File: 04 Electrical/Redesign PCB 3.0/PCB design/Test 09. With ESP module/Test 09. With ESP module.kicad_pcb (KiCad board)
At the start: 2 copper layers, 90 x 54 mm, 69 parts, among them J1 USB-C port, J2 Boiler, J3 Test connector, Q1 MMBT2907A, Q2 LBSS138LT1G-ES, SW1 btn_home, SW2 btn_up, SW3 btn_down, SW4 btn_confirm, SW5 btn_back, U1 ESP32-S3-WROOM-1-N8R2, U10 LP5907MFX-2.8/NOPB, U11 VL53L0CXV0DH/1, U2 SGM2212-3.3XKC3G/TR, U3 EL357N-G, U4 EL357N-G, U5 ILI9341_no_touch, U6 DS18S20, U7 DS18S20, U8 DS18S20, U9 DS18S20

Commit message: Routing PCB test 9
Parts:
- removed C13: 10u, Capacitor_SMD:C_0402_1005Metric
- removed C14: 0.1u, Capacitor_SMD:C_0603_1608Metric
- removed C15: 4.7pF, Capacitor_SMD:C_0603_1608Metric
- removed D18, D19, D20: WS2812B-2020, LED_SMD:LED_WS2812B_PLCC4_5.0x5.0mm_P3.2mm
- removed Q2: LBSS138LT1G-ES, Package_TO_SOT_SMD:SOT-23
- removed R11, R12, R13: 10k, Resistor_SMD:R_0603_1608Metric
- removed U10: LP5907MFX-2.8/NOPB, Package_TO_SOT_SMD:SOT-23-5
- removed U11: VL53L0CXV0DH/1, Sensor_Distance:ST_VL53L1x
- added J4: VL6180, Connector_PinHeader_2.00mm:PinHeader_1x06_P2.00mm_Vertical, F.Cu at (169.5, 50.5)
- J3: footprint Project:PinHeader_1x04_P2.54mm_Horizontal -> Connector_PinHeader_2.54mm:PinHeader_1x06_P2.54mm_Vertical
- U3, U4: footprint EL357N-G:OPTO_EL357N-G -> Package_SO:SOP-4_3.8x4.1mm_P2.54mm
- moved J3 10.8 mm to (148.4, 99.8)
- moved R3 7.41 mm to (118.0, 96.5), turned to 0 degrees
- moved R2 7.35 mm to (132.8, 96.8), turned to 180 degrees
- moved J2 6.97 mm to (167.7, 98.6)
- moved C10 5.76 mm to (160.8, 87.6)
- moved D11 5.76 mm to (163.3, 87.6)
- moved D6 5.76 mm to (155.1, 94.3)
- moved D8 5.76 mm to (160.1, 94.3)
- moved Q1 5.76 mm to (154.8, 87.6)
- moved R7 5.76 mm to (158.3, 87.6)
- moved C11 5.76 mm to (150.0, 80.7)
- moved C12 5.76 mm to (166.0, 81.0)
- moved C9 5.76 mm to (149.9, 87.9)
- moved D10 5.76 mm to (149.9, 90.4)
- moved D12 5.76 mm to (167.6, 90.3)
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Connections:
- D6 pad 2: Net-(D6-A) -> Boiler 1
- D7 pad 1: Net-(D6-A) -> Boiler 1
- D8 pad 2: Net-(D8-A) -> Boiler 2
- D9 pad 1: Net-(D8-A) -> Boiler 2
- J2 pad 1: Net-(D6-A) -> Boiler 1
- J2 pad 2: Net-(D8-A) -> Boiler 2
- U1 pad 11: Disp_LED -> unconnected-(U1-GPIO18/U1RXD/ADC2_CH7/CLK_OUT3-Pad11)
- U1 pad 15: Disp_CS -> Disp_LED
- U1 pad 16: Disp_MISO -> unconnected-(U1-GPIO46-Pad16)
- U1 pad 17: Disp_SCK -> unconnected-(U1-GPIO9/TOUCH9/ADC1_CH8/FSPIHD/SUBSPIHD-Pad17)
- U1 pad 18: Disp_MOSI -> unconnected-(U1-GPIO10/TOUCH10/ADC1_CH9/FSPICS0/FSPIIO4/SUBSPICS0-Pad18)
- U1 pad 19: unconnected-(U1-GPIO11/TOUCH11/ADC2_CH0/FSPID/FSPIIO5/SUBSPID-Pad19) -> Disp_MOSI
- U1 pad 20: TOF_SCL -> Disp_SCK
- U1 pad 21: TOF_XSHUT -> Disp_MISO
- U1 pad 22: TOF_GPIO01 -> unconnected-(U1-GPIO14/TOUCH14/ADC2_CH3/FSPIWP/FSPIDQS/SUBSPIWP-Pad22)
- U1 pad 23: TOF_SDA -> unconnected-(U1-GPIO21-Pad23)
- U1 pad 27: unconnected-(U1-GPIO0/BOOT-Pad27) -> btn_back
- U1 pad 28: unconnected-(U1-SPIIO6/GPIO35/FSPID/SUBSPID-Pad28) -> btn_confirm
- U1 pad 29: unconnected-(U1-SPIIO7/GPIO36/FSPICLK/SUBSPICLK-Pad29) -> SD_CS
- U1 pad 30: btn_back -> SD_MOSI
- U1 pad 31: btn_confirm -> SD_MISO
- U1 pad 32: SD_CS -> SD_SCK
- U1 pad 33: SD_MOSI -> btn_down
- U1 pad 34: SD_MISO -> btn_up
- U1 pad 35: SD_SCK -> btn_home
- U1 pad 36: btn_down -> TOF_SDA
- U1 pad 37: btn_up -> TOF_SCL
- U1 pad 38: btn_home -> TOF_GPIO01
- U1 pad 39: WS2812_CTRL -> TOF_XSHUT
- U1 pad 7: Disp_RES -> Disp_CS
- U1 pad 8: Disp_DC -> Disp_RES
- U1 pad 9: unconnected-(U1-GPIO16/U0CTS/ADC2_CH5/XTAL_32K_N-Pad9) -> Disp_DC
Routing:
- net VCC_5V: track 123.5 -> 46.6 mm, vias 2 -> 1
- net Boiler 1: track 0.00 -> 45.1 mm, vias 0 -> 2
- net VCC_3V3: track 298.6 -> 260.4 mm, vias 13 -> 6
- net Boiler 2: track 0.00 -> 37.9 mm, vias 0 -> 2
- net Net-(U10-OUT): track 23.4 -> 0.00 mm
- net Net-(D6-A): track 22.1 -> 0.00 mm
- net WS2812_CTRL: track 22.0 -> 0.00 mm
- net Net-(D8-A): track 14.5 -> 0.00 mm
- net Net-(D18-DIN): track 7.28 -> 0.00 mm
- net TOF_GPIO01: track 42.7 -> 36.0 mm
- net boil_to_cntr: track 38.8 -> 32.3 mm
- net btn_down: track 64.6 -> 58.1 mm
- net Net-(D18-DOUT): track 5.51 -> 0.00 mm
- net Net-(D19-DOUT): track 5.43 -> 0.00 mm
- net TOF_SDA: track 45.0 -> 40.3 mm
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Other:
- board text added: "Boiler 1"
- board text added: "Boiler 2"
- board text added: "GPIO01"
- board text added: "SCL"
- board text added: "SDA"
- board text added: "XSHUT"

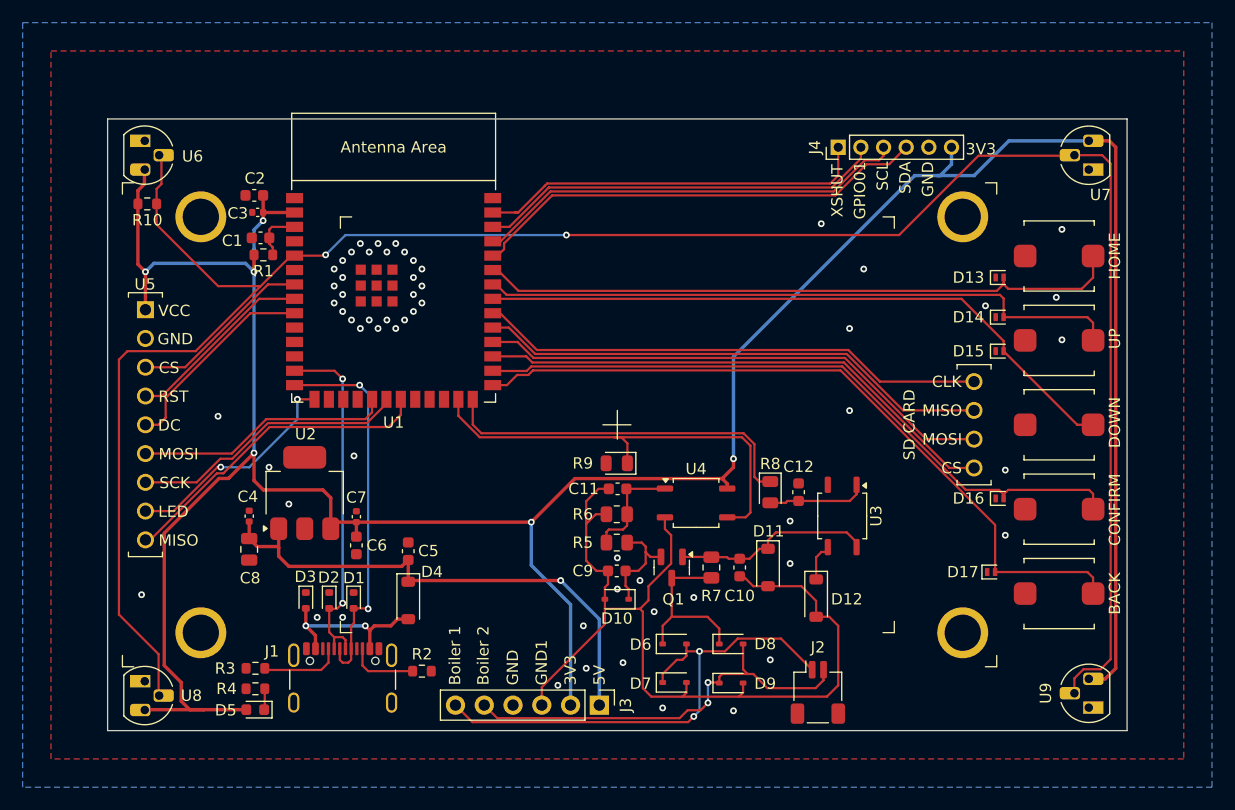
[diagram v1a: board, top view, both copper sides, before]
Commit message: Logo added to PCB
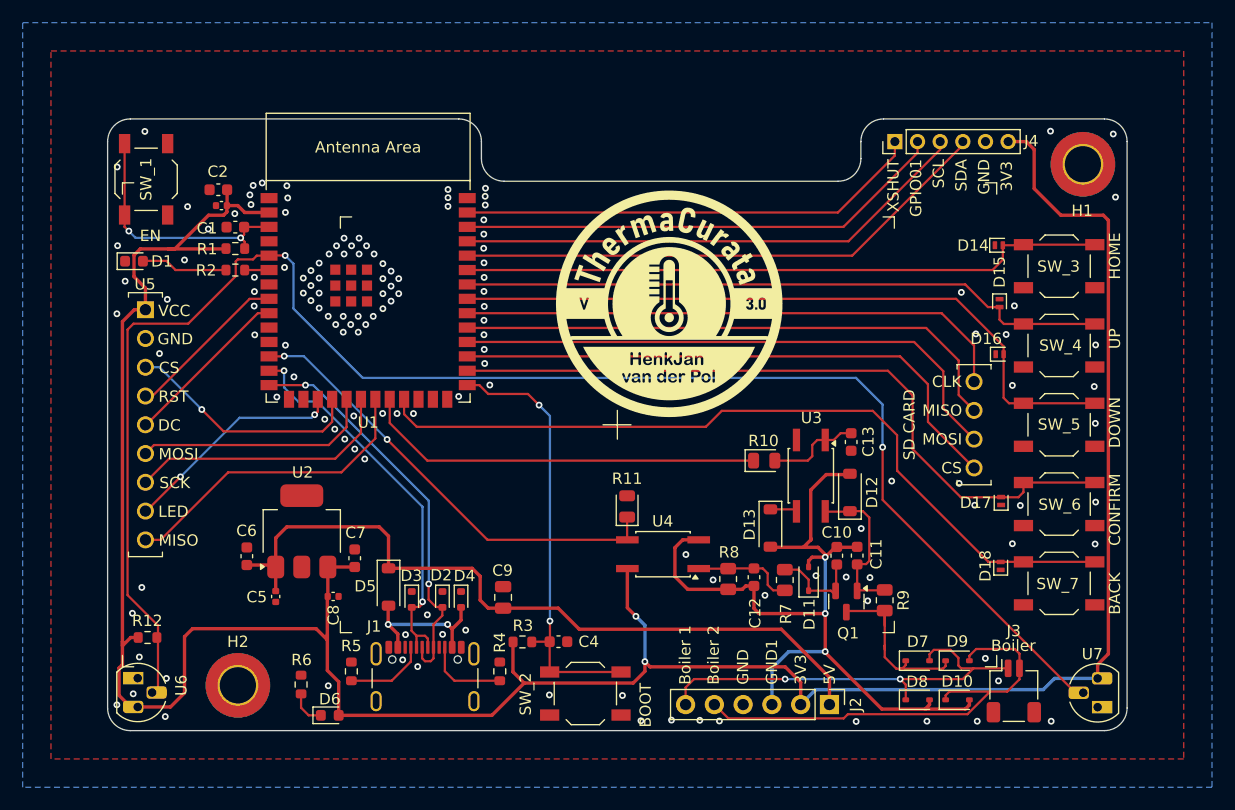
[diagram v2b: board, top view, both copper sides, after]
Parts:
- removed SW1: btn_home, Project:SW_Push_SPEH
- removed SW2: btn_up, Project:SW_Push_SPEH
- removed SW3: btn_down, Project:SW_Push_SPEH
- removed SW4: btn_confirm, Project:SW_Push_SPEH
- removed SW5: btn_back, Project:SW_Push_SPEH
- removed U8, U9: DS18S20, Package_TO_SOT_THT:TO-92L_HandSolder
- added C13: 2n2, Capacitor_SMD:C_0603_1608Metric, F.Cu at (170.6, 76.5)
- added D18: LESD8D3.3CAT5G-ES, Diode_SMD:D_SOD-882, F.Cu at (183.8, 87.5)
- added H1: MountingHole_Pad, MountingHole:MountingHole_3.2mm_M3_ISO7380_Pad_TopBottom, F.Cu at (191.1, 52.0)
- added H2: MountingHole_Pad, MountingHole:MountingHole_3.2mm_M3_ISO7380_Pad_TopBottom, F.Cu at (116.5, 98.0)
- added R11: 330, Diode_SMD:D_0805_2012Metric, F.Cu at (150.9, 82.2)
- added R12: 4k7, Resistor_SMD:R_0603_1608Metric, F.Cu at (108.5, 93.8)
- added SW_1: EN, Button_Switch_SMD:SW_SPST_TL3342, F.Cu at (108.4, 53.3)
- added SW_2: BOOT, Button_Switch_SMD:SW_SPST_TL3342, F.Cu at (147.2, 98.7)
- added SW_3: HOME, Button_Switch_SMD:SW_SPST_TL3342, F.Cu at (189.0, 61.0)
- added SW_4: UP, Button_Switch_SMD:SW_SPST_TL3342, F.Cu at (189.0, 68.0)
- added SW_5: DOWN, Button_Switch_SMD:SW_SPST_TL3342, F.Cu at (189.0, 75.0)
- added SW_6: CONFIRM, Button_Switch_SMD:SW_SPST_TL3342, F.Cu at (189.0, 82.0)
- added SW_7: BACK, Button_Switch_SMD:SW_SPST_TL3342, F.Cu at (189.0, 89.0)
- C10, C12: value 2n2 -> 10n
- C11: value 10n -> 2n2
- C4: value 10u -> 1u; footprint Capacitor_SMD:C_0402_1005Metric -> Capacitor_SMD:C_0603_1608Metric
- C5: value 0.1u -> 10u; footprint Capacitor_SMD:C_0603_1608Metric -> Capacitor_SMD:C_0402_1005Metric
- C7: value 10u -> 0.1u; footprint Capacitor_SMD:C_0402_1005Metric -> Capacitor_SMD:C_0603_1608Metric
- C8: value 22u -> 10u; footprint Capacitor_SMD:C_0805_2012Metric -> Capacitor_SMD:C_0402_1005Metric
- C9: value 10n -> 22u; footprint Capacitor_SMD:C_0603_1608Metric -> Capacitor_SMD:C_0805_2012Metric
- D1: value LESD5D5.0CT1G -> XL-1608UGC-04; footprint Diode_SMD:D_SOD-523 -> LED_SMD:LED_0603_1608Metric
- D10: value BZT52C4V7S -> 1N4148WS
- D11: value BZT52C15V -> BZT52C4V7S; footprint Diode_SMD:D_SOD-123 -> Diode_SMD:D_SOD-323
- D12: value BZT52C4V3 -> BZT52C15V
- D13: value LESD8D3.3CAT5G-ES -> BZT52C4V3; footprint Diode_SMD:D_SOD-882 -> Diode_SMD:D_SOD-123
- D4: value 1N5819HW-7-F -> LESD5D5.0CT1G; footprint Diode_SMD:D_SOD-123 -> Diode_SMD:D_SOD-523
- D5: value XL-1608UGC-04 -> 1N5819HW-7-F; footprint LED_SMD:LED_0603_1608Metric -> Diode_SMD:D_SOD-123
- D6: value 1N4148WS -> XL-1608UGC-04; footprint Diode_SMD:D_SOD-323 -> LED_SMD:LED_0603_1608Metric
- J2: value Boiler -> Test connector; footprint Connector_JST:JST_SH_SM02B-SRSS-TB_1x02-1MP_P1.00mm_Horizontal -> Connector_PinHeader_2.54mm:PinHeader_1x06_P2.54mm_Vertical
- J3: value Test connector -> Boiler; footprint Connector_PinHeader_2.54mm:PinHeader_1x06_P2.54mm_Vertical -> Connector_JST:JST_SH_SM02B-SRSS-TB_1x02-1MP_P1.00mm_Horizontal
- R10: value 4k7 -> 1k5; footprint Resistor_SMD:R_0603_1608Metric -> Diode_SMD:D_0805_2012Metric
- R2: value 4k7 -> 5k1
- R3: value 4k7 -> 10k
- R4: value 5k1 -> 4k7
- R5: value 200 -> 4k7; footprint Resistor_SMD:R_0805_2012Metric -> Resistor_SMD:R_0603_1608Metric
- R6: value 150 -> 5k1; footprint Resistor_SMD:R_0805_2012Metric -> Resistor_SMD:R_0603_1608Metric
- R7: value 330 -> 200
- R8: value 1k5 -> 150; footprint Diode_SMD:D_0805_2012Metric -> Resistor_SMD:R_0805_2012Metric
- R9: footprint Diode_SMD:D_0805_2012Metric -> Resistor_SMD:R_0805_2012Metric
- U3, U4: footprint Package_SO:SOP-4_3.8x4.1mm_P2.54mm -> Package_SO:SO-4_4.4x3.6mm_P2.54mm
- U5: footprint Project:ILI9341_no_touch -> Project:ILI9341_no_touch_no_mount
- moved R10 59.0 mm to (163.0, 78.2), turned to 0 degrees
- moved U7 47.5 mm to (192.4, 99.9)
- moved U6 47.4 mm to (107.7, 97.4)
- moved R2 39.1 mm to (116.3, 61.3), turned to 0 degrees
- moved J3 36.6 mm to (185.0, 98.5), turned to 0 degrees
- moved D1 35.7 mm to (107.3, 60.6), turned to 0 degrees
- moved R6 31.7 mm to (122.1, 97.9), turned to -90 degrees
- moved D10 31.4 mm to (180.0, 99.3), turned to 0 degrees
- moved D6 31.1 mm to (124.6, 100.7)
- moved D13 30.0 mm to (163.5, 84.1), turned to -90 degrees
- moved C4 29.5 mm to (144.8, 94.2), turned to 0 degrees
- moved R9 26.6 mm to (173.6, 90.5), turned to -90 degrees
- moved R5 26.0 mm to (126.5, 96.8), turned to -90 degrees
- moved R3 23.7 mm to (141.6, 94.2)
- moved C11 22.0 mm to (171.2, 86.5), turned to 90 degrees
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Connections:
- C10 pad 1: Net-(D11-K) -> GND1
- C10 pad 2: GND1 -> Net-(D11-K)
- C11 pad 1: GND1 -> Net-(D12-K)
- C11 pad 2: Net-(C11-Pad2) -> GND1
- C12 pad 1: GND -> GND1
- C4 pad 1: VCC_5V -> Net-(U1-GPIO0/BOOT)
- C6 pad 1: VCC_3V3 -> VCC_5V
- C8 pad 1: VCC_5V -> VCC_3V3
- C9 pad 1: GND1 -> VCC_5V
- C9 pad 2: Net-(D10-K) -> GND
- D1 pad 2: USB D+ -> Net-(D1-A)
- D10 pad 1: Net-(D10-K) -> Boiler 2
- D13 pad 1: GND -> Net-(D13-K)
- D13 pad 2: btn_home -> GND1
- D14 pad 2: btn_up -> btn_home
- D15 pad 2: btn_down -> btn_up
- D16 pad 2: btn_confirm -> btn_down
- D17 pad 2: btn_back -> btn_confirm
- D2 pad 2: USB D- -> USB D+
- D3 pad 2: Vusb -> USB D-
- D4 pad 1: VCC_5V -> GND
- D5 pad 1: Net-(D5-K) -> VCC_5V
- D5 pad 2: VCC_3V3 -> Vusb
- D6 pad 2: Boiler 1 -> VCC_3V3
- D7 pad 1: Boiler 1 -> Net-(D7-K)
- D7 pad 2: GND1 -> Boiler 1
- D8 pad 1: Net-(D6-K) -> Boiler 1
- D8 pad 2: Boiler 2 -> GND1
- D9 pad 1: Boiler 2 -> Net-(D7-K)
- D9 pad 2: GND1 -> Boiler 2
- J2 pad 1: Boiler 1 -> VCC_5V
- J2 pad 2: Boiler 2 -> VCC_3V3
- J3 pad 1: VCC_5V -> Boiler 1
- J3 pad 2: VCC_3V3 -> Boiler 2
- Q1 pad 1: Net-(D11-K) -> Net-(D12-K)
- Q1 pad 2: Net-(D10-K) -> Net-(D11-K)
- Q1 pad 3: Net-(D6-K) -> Net-(D7-K)
- R1 pad 1: Net-(U1-EN) -> VCC_3V3
- R1 pad 2: VCC_3V3 -> Net-(U1-EN)
- R10 pad 1: onewire -> boil_to_cntr
- R10 pad 2: VCC_3V3 -> Net-(C13-Pad2)
- R2 pad 1: GND -> Net-(D1-A)
- R2 pad 2: Net-(J1-CC2) -> Net-(U1-GPIO6/TOUCH6/ADC1_CH5)
- R3 pad 1: GND -> VCC_3V3
- R3 pad 2: Net-(J1-CC1) -> Net-(U1-GPIO0/BOOT)
- R4 pad 2: Net-(D5-K) -> Net-(J1-CC2)
- R5 pad 1: Net-(D10-K) -> GND
- R5 pad 2: Net-(C11-Pad2) -> Net-(J1-CC1)
- R6 pad 1: Net-(C11-Pad2) -> GND
- R6 pad 2: GND1 -> Net-(D6-K)
- R7 pad 2: Net-(D6-K) -> Net-(C12-Pad2)
- R8 pad 1: boil_to_cntr -> Net-(C12-Pad2)
- R8 pad 2: Net-(C12-Pad2) -> GND1
- R9 pad 1: cntr_to_boil -> Net-(D12-K)
- R9 pad 2: GND -> Net-(D7-K)
- U1 pad 12: unconnected-(U1-GPIO8/TOUCH8/ADC1_CH7/SUBSPICS1-Pad12) -> cntr_to_boil
- U1 pad 15: Disp_LED -> unconnected-(U1-GPIO3/TOUCH3/ADC1_CH2-Pad15)
- U1 pad 17: unconnected-(U1-GPIO9/TOUCH9/ADC1_CH8/FSPIHD/SUBSPIHD-Pad17) -> Disp_LED
- U1 pad 18: unconnected-(U1-GPIO10/TOUCH10/ADC1_CH9/FSPICS0/FSPIIO4/SUBSPICS0-Pad18) -> Disp_CS
- U1 pad 22: unconnected-(U1-GPIO14/TOUCH14/ADC2_CH3/FSPIWP/FSPIDQS/SUBSPIWP-Pad22) -> boil_to_cntr
- U1 pad 23: unconnected-(U1-GPIO21-Pad23) -> btn_back
- U1 pad 25: cntr_to_boil -> unconnected-(U1-GPIO48/SPICLK_N/SUBSPICLK_N_DIFF-Pad25)
- U1 pad 26: boil_to_cntr -> unconnected-(U1-GPIO45-Pad26)
- U1 pad 27: btn_back -> Net-(U1-GPIO0/BOOT)
- U1 pad 6: unconnected-(U1-GPIO6/TOUCH6/ADC1_CH5-Pad6) -> Net-(U1-GPIO6/TOUCH6/ADC1_CH5)
- U1 pad 7: Disp_CS -> unconnected-(U1-GPIO7/TOUCH7/ADC1_CH6-Pad7)
- U3 pad 1: Net-(C12-Pad2) -> Net-(C13-Pad2)
- U3 pad 3: Net-(D12-K) -> Net-(D13-K)
- U3 pad 4: Net-(D11-K) -> Net-(D12-K)
- U4 pad 1: Net-(C11-Pad2) -> Net-(C12-Pad2)
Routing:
- net onewire: track 192.5 -> 143.7 mm
- net Net-(U1-GPIO0/BOOT): track 0.00 -> 38.8 mm, vias 0 -> 2
- net VCC_5V: track 46.6 -> 67.2 mm, vias 1 -> 0
- net Net-(U1-EN): track 4.69 -> 23.1 mm, vias 0 -> 2
- net Net-(D7-K): track 0.00 -> 16.3 mm
- net VCC_3V3: track 260.4 -> 245.5 mm, vias 6 -> 2
- net Net-(D6-K): track 15.6 -> 3.25 mm
- net Net-(D12-K): track 3.18 -> 13.4 mm
- net Net-(D10-K): track 9.46 -> 0.00 mm
- net Net-(D11-K): track 17.2 -> 7.90 mm
- net Net-(C11-Pad2): track 9.12 -> 0.00 mm
- net GND1: track 83.0 -> 74.4 mm, vias 0 -> 3
- net Net-(C13-Pad2): track 0.00 -> 8.32 mm
- net TOF_SDA: track 40.3 -> 47.8 mm
- net TOF_GPIO01: track 36.0 -> 43.4 mm
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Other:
- outline, holes or cut-outs redrawn
- board text added: "BOOT"
- board text added: "Boiler"
- board text added: "EN"

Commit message: As ordered at JLCPCB
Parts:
- removed C10, C12: 10n, Capacitor_SMD:C_0603_1608Metric
- removed C11, C13: 2n2, Capacitor_SMD:C_0603_1608Metric
- removed J4: VL6180, Connector_PinHeader_2.00mm:PinHeader_1x06_P2.00mm_Vertical
- added TP1: 5V, TestPoint:TestPoint_Keystone_5015_Micro-Minature, F.Cu at (159.8, 97.8)
- added TP2: 3V3, TestPoint:TestPoint_Keystone_5015_Micro-Minature, F.Cu at (155.7, 97.8)
- added TP3: GND1, TestPoint:TestPoint_Keystone_5015_Micro-Minature, F.Cu at (171.9, 97.8)
- added TP4: GND, TestPoint:TestPoint_Keystone_5015_Micro-Minature, F.Cu at (163.8, 97.8)
- added TP5: opnthm, TestPoint:TestPoint_Keystone_5015_Micro-Minature, F.Cu at (167.9, 97.8)
- added TP6: B1, TestPoint:TestPoint_Keystone_5015_Micro-Minature, F.Cu at (176.0, 97.8)
- added TP7: B2, TestPoint:TestPoint_Keystone_5015_Micro-Minature, F.Cu at (180.1, 97.8)
- D2, D3, D4: value LESD5D5.0CT1G -> BSD5C051L
- J2: value Test connector -> Boiler; footprint Connector_PinHeader_2.54mm:PinHeader_1x06_P2.54mm_Vertical -> Connector_JST:JST_SH_SM02B-SRSS-TB_1x02-1MP_P1.00mm_Horizontal
- J3: value Boiler -> VL6180; footprint Connector_JST:JST_SH_SM02B-SRSS-TB_1x02-1MP_P1.00mm_Horizontal -> Connector_PinHeader_2.00mm:PinHeader_1x06_P2.00mm_Vertical
- R11: footprint Diode_SMD:D_0805_2012Metric -> Resistor_SMD:R_0805_2012Metric
- R7: value 200 -> 180
- R8: value 150 -> 100
- U2: value SGM2212-3.3XKC3G/TR -> UZ1086L-33-TN3-R; footprint Package_TO_SOT_SMD:SOT-223-3_TabPin2 -> Package_TO_SOT_SMD:TO-252-2
- moved J3 48.9 mm to (174.8, 50.6), turned to 90 degrees
- moved J2 17.1 mm to (185.8, 98.5), turned to 0 degrees
- moved D10 10.2 mm to (180.8, 89.1), turned to 90 degrees
- moved D8 7.89 mm to (180.8, 92.7), turned to 90 degrees
- moved D9 7.21 mm to (177.3, 89.1), turned to 90 degrees
- moved C5 6.62 mm to (113.2, 90.1), turned to 90 degrees
- moved R11 5.88 mm to (149.5, 87.9), turned to -90 degrees
- moved C6 3.99 mm to (114.9, 89.8)
- moved C7 3.92 mm to (124.5, 89.9)
- moved D7 3.28 mm to (177.3, 92.7), turned to 90 degrees
- moved D12 3.18 mm to (170.6, 84.2)
- moved U2 2.71 mm to (119.7, 85.6)
- moved U4 2.41 mm to (155.6, 88.3)
- moved C8 1.79 mm to (126.6, 90.7)
- moved R8 1.57 mm to (161.4, 88.6), turned to 90 degrees
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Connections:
- net Net-(C12-Pad2) renamed boiler
- J2 pad 1: VCC_5V -> Boiler 1
- J2 pad 2: VCC_3V3 -> Boiler 2
- J3 pad 1: Boiler 1 -> TOF_XSHUT
- J3 pad 2: Boiler 2 -> TOF_GPIO01
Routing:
- net GND1: track 74.4 -> 0.00 mm, vias 3 -> 13
- net Boiler 2: track 40.9 -> 21.3 mm
- net Boiler 1: track 38.4 -> 19.0 mm, vias 2 -> 0
- net VCC_5V: track 67.2 -> 55.5 mm
- net VCC_3V3: track 245.5 -> 238.7 mm, vias 2 -> 5
- net boiler: track 8.97 -> 15.4 mm
- net Net-(D7-K): track 16.3 -> 11.1 mm
- net onewire: track 143.7 -> 148.2 mm
- net Net-(D12-K): track 13.4 -> 10.1 mm
- net Net-(D11-K): track 7.90 -> 5.65 mm
- net Net-(U1-GPIO0/BOOT): track 38.8 -> 36.7 mm
- net TOF_SDA: track 47.8 -> 49.8 mm
- net Net-(R10-Pad2): track 8.32 -> 6.56 mm
- net GND: track 0.00 -> 1.64 mm, vias 142 -> 187
- net Net-(D13-K): track 2.12 -> 3.60 mm
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- added copper zone on B.Cu, net GND1
- added copper zone on F.Cu, net GND1
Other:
- board text added: "https://github.com/henkjannl/RoomThermostat"
- board text removed: "5V"
- board text removed: "BACK"
- board text removed: "BOOT"
- board text removed: "Boiler"
- board text removed: "Boiler 1"
- board text removed: "Boiler 2"
- board text removed: "CONFIRM"
- board text removed: "DOWN"
- board text removed: "EN"
- board text removed: "GND1"
- board text removed: "HOME"
- board text removed: "UP"
